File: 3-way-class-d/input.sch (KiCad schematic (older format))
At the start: 12 parts

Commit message: More input
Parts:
- added C?: RCA, symbol RCA
- added C?: 47n, symbol C_Small
- added C?: C_Small, symbol C_Small
- added D?: blue, symbol Led_Small
- added JP?: Jumper_NO_Small, symbol Jumper_NO_Small
- added Q?: BC857, SOT-23, symbol BC857
- added R? (x4): 47, symbol R_Small
- added R? (x2): 100, symbol R_Small
- added R?: 4.7k, symbol R_Small
- added R?: 392, symbol R_Small
- added R?: 4.99k, symbol R_Small
- added R?: 75, symbol R_Small
- added R?: 1M, symbol R_Small
- added R?: 2k, symbol R_Small
- added R?: 7.5k, symbol R_Small
- added U?: SN74LVC2G157, symbol SN74LVC2G157
- added U?: PLR135, symbol PLR135
- added U? (x2): 74HC1GU04, symbol 74HC1GU04
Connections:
- net labels added: LRCLK, MCLK, SCLK, SDATA1
- wire segments 23 -> 82
- no-connect marks 0 -> 9
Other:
- note added: "closed: SCKO 512 frames\nopen: SCKO 256 frames"
- moved on the sheet: C?, R?

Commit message: ADC
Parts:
- added JP1, JP2: Jumper_NO_Small, symbol Jumper_NO_Small
- added R1: 4.99k, symbol R_Small
- gave numbers to parts that had none: 35
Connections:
- net +3V3: now also R1.2
- net GNDPWR: now also JP2.1
- net DSEL: now reaches U2.6 (~A~/B)
- net DSEL: now also JP1.2, JP2.2
- new net: JP1.1, R1.1
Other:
- note added: "jp1: opto\njp2: coax"
- moved on the sheet: C4, C5, C6, C7, D1, JP3, JP4, JP5, Q1, R10, R11, R12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

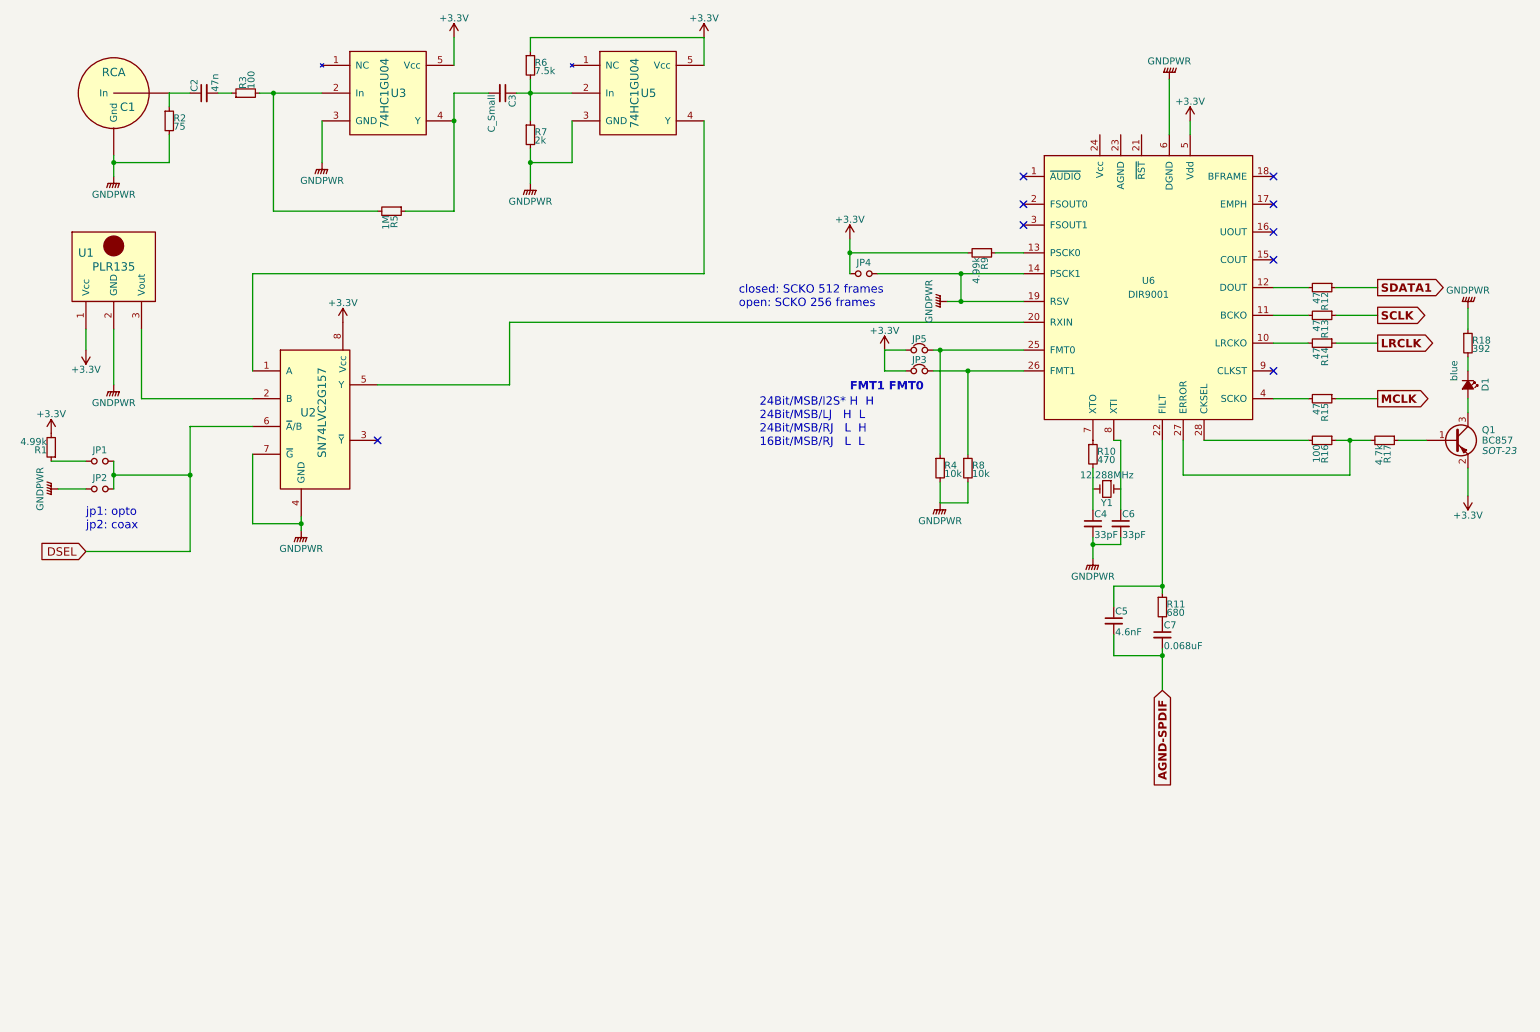
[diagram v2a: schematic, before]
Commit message: Add peak_detect
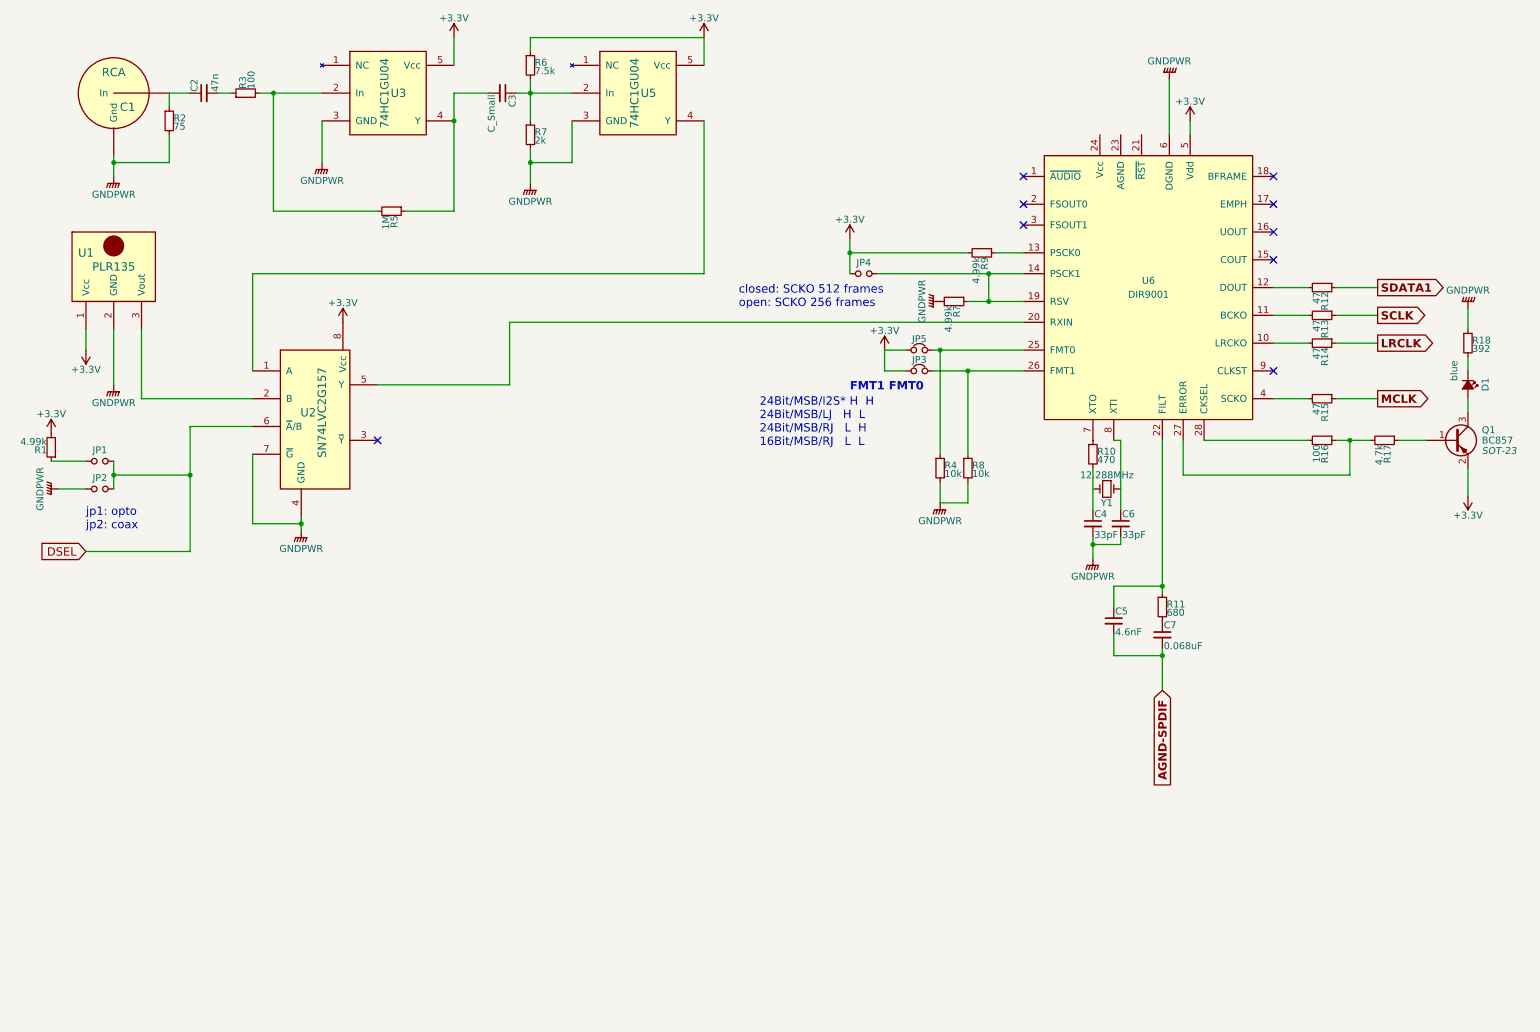
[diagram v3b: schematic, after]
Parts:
- added R?: 4.99k, symbol R_Small
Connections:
- net GNDPWR: now also R?.2; no longer JP4.2, U6.14 (PSCK1), U6.19 (RSV)
- new net: JP4.2, R?.1, U6.14 (PSCK1), U6.19 (RSV)
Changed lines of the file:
@@
 L GNDPWR #PWR16
 U 1 1 57A9F4AD
-P 7150 2600
-F 0 "#PWR16" H 7150 2400 50  0001 C CNN
-F 1 "GNDPWR" H 7150 2470 50  0000 C CNN
-F 2 "" H 7150 2550 60  0000 C CNN
-F 3 "" H 7150 2550 60  0000 C CNN
-	1    7150 2600
+P 7100 2600
+F 0 "#PWR16" H 7100 2400 50  0001 C CNN
+F 1 "GNDPWR" H 7100 2470 50  0000 C CNN
+F 2 "" H 7100 2550 60  0000 C CNN
+F 3 "" H 7100 2550 60  0000 C CNN
+	1    7100 2600
 	0    1    1    0
 $EndComp
@@
 DSEL
 Wire Wire Line
-	7050 2950 7100 2950
-Wire Wire Line
-	7100 2950 7700 2950
-Wire Wire Line
-	7050 3100 7300 3100
-Wire Wire Line
-	7300 3100 7700 3100
+	7050 2950 7700 2950
+Wire Wire Line
+	7050 3100 7700 3100
 Wire Wire Line
 	6850 2950 6700 2950
@@
 	7300 4050 7300 3900
 Wire Wire Line
-	8700 3600 8700 4650
-Wire Wire Line
-	8700 4650 8700 4700
+	8700 3600 8700 4700
 Wire Wire Line
 	8200 3800 8200 4100
@@
 Connection ~ 8700 4650
 Wire Wire Line
-	8700 5100 8700 5150
-Wire Wire Line
-	8700 5150 8700 5400
+	8700 5100 8700 5400
 Wire Wire Line
 	8350 5150 8700 5150
 Connection ~ 8700 5150
 Wire Wire Line
-	8200 4300 8200 4350
-Wire Wire Line
-	8200 4350 8200 4450
+	8200 4300 8200 4450
 Wire Wire Line
 	8400 4300 8400 4350
@@
 Connection ~ 8200 4350
 Wire Wire Line
-	7150 2600 7250 2600
-Wire Wire Line
-	7250 2600 7700 2600
+	7300 2600 7700 2600
 Wire Wire Line
 	8750 1000 8750 1400
@@
 	10600 3600 10400 3600
 Wire Wire Line
-	9950 3600 10050 3600
-Wire Wire Line
-	10050 3600 10200 3600
+	9950 3600 10200 3600
 Wire Wire Line
 	10900 2650 10900 2800
@@
 Connection ~ 10050 3600
 Wire Wire Line
-	6450 2150 6450 2250
-Wire Wire Line
-	6450 2250 6450 2400
+	6450 2150 6450 2400
 Connection ~ 6450 2250
 Wire Wire Line
@@
 	7300 2250 6450 2250
 Wire Wire Line
-	6650 2400 7250 2400
-Wire Wire Line
-	7250 2400 7700 2400
-Wire Wire Line
-	7250 2600 7250 2400
-Connection ~ 7250 2400
-Connection ~ 7250 2600
+	6650 2400 7700 2400
+Connection ~ 7450 2400
+Connection ~ 7450 2600
 Wire Wire Line
 	4000 2750 7700 2750
 Wire Wire Line
-	2500 4150 2500 4200
-Wire Wire Line
-	2500 4200 2500 4250
+	2500 4150 2500 4250
 Wire Wire Line
 	2150 3700 2150 4200
@@
 	950  2800 950  2950
 Wire Wire Line
-	1150 1550 1150 1600
-Wire Wire Line
-	1150 1600 1150 1700
+	1150 1550 1150 1700
 Wire Wire Line
 	1550 1400 1550 1600
@@
 	2650 1300 2650 1600
 Wire Wire Line
-	2200 1100 2300 1100
-Wire Wire Line
-	2300 1100 2650 1100
+	2200 1100 2650 1100
 Wire Wire Line
 	3600 900  3600 700
 Wire Wire Line
-	3600 1100 3600 1300
-Wire Wire Line
-	3600 1300 3600 1950
+	3600 1100 3600 1950
 Wire Wire Line
 	3600 1950 3250 1950
@@
 	1350 3300 2150 3300
 Wire Wire Line
-	4050 1100 4150 1100
-Wire Wire Line
-	4150 1100 4450 1100
-Wire Wire Line
-	4150 1000 4150 1100
-Wire Wire Line
-	4150 1100 4150 1300
+	4050 1100 4450 1100
+Wire Wire Line
+	4150 1000 4150 1300
 Connection ~ 4150 1100
 Wire Wire Line
@@
 Connection ~ 3600 1300
 Wire Wire Line
-	4150 1500 4150 1600
-Wire Wire Line
-	4150 1600 4150 1750
+	4150 1500 4150 1750
 Wire Wire Line
 	4450 1300 4450 1600
@@
 	2150 3500 1700 3500
 Wire Wire Line
-	1150 3750 1150 3850
-Wire Wire Line
-	1150 3850 1150 3950
+	1150 3750 1150 3950
 Connection ~ 1150 3850
 Wire Wire Line
@@
 	1150 3850 1700 3850
 Wire Wire Line
-	1700 3500 1700 3850
-Wire Wire Line
-	1700 3850 1700 4400
+	1700 3500 1700 4400
 Wire Wire Line
 	1700 4400 950  4400
 Connection ~ 1700 3850
+Wire Wire Line
+	7450 2600 7450 2400
+$Comp
+L R_Small R?
+U 1 1 58C2DF75
+P 7200 2600
+F 0 "R?" H 7230 2620 50  0000 L CNN
+F 1 "4.99k" H 7230 2560 50  0000 L CNN
+F 2 "" H 7200 2600 60  0000 C CNN
+F 3 "" H 7200 2600 60  0000 C CNN
+	1    7200 2600
+	0    1    1    0
+$EndComp
 $EndSCHEMATC

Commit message: Update remaining projects to KiCad 5
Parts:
- C1: symbol RCA -> lci-kicad:RCA
- C2, C3, C4, C5, C6, C7: symbol C_Small -> device:C_Small
- D1: symbol Led_Small -> device:LED_Small
- JP1, JP2, JP4: symbol Jumper_NO_Small -> device:Jumper_NO_Small
- JP3, JP5: symbol Jumper_NC_Small -> device:Jumper_NC_Small
- Q1: symbol BC857 -> Transistor:BC857
- R1, R10, R11, R12, R13, R14, R15, R16, R17, R18, R2, R3, R4, R5, R6, R7, R8, R9, R?: symbol R_Small -> device:R_Small
- U1: symbol PLR135 -> lci-kicad:PLR135
- U2: symbol SN74LVC2G157 -> lci-kicad:SN74LVC2G157
- U3, U5: symbol 74HC1GU04 -> lci-kicad:74HC1GU04
- U6: symbol DIR9001 -> lci-kicad:DIR9001
- Y1: symbol Crystal_Small -> device:Crystal_Small
